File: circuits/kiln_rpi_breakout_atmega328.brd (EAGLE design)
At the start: 65 x 56 mm, 31 parts, among them Q1 5A, U1 INA125P

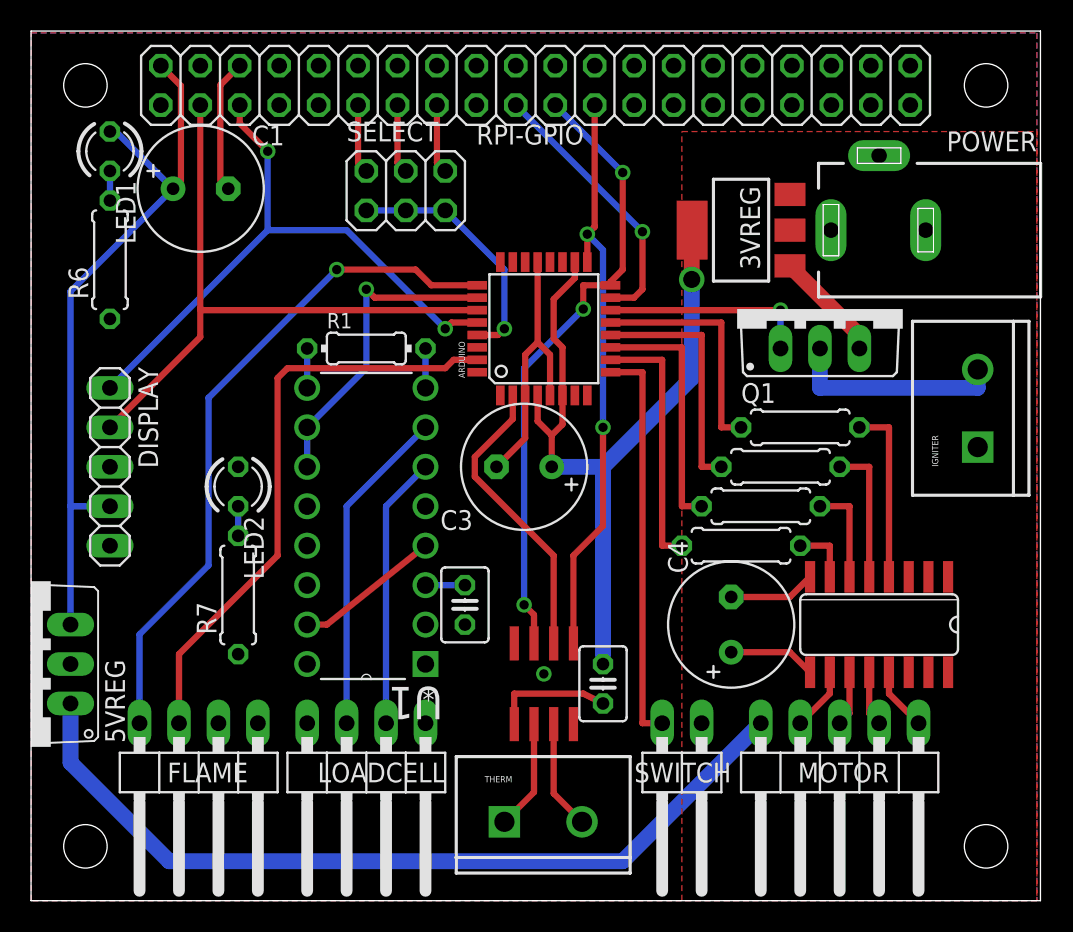
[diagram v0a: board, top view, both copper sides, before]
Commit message: Add auxtemp header, stacking power connector
Managed to update the pcb order in time. Auxtemp header takes a DS18B20
chip as an auxiliary temperature monitor, good for checking for propane
tank freezing or even as primary temperature control. Additional
powerstack header allows stacked breakouts to pass power between boards
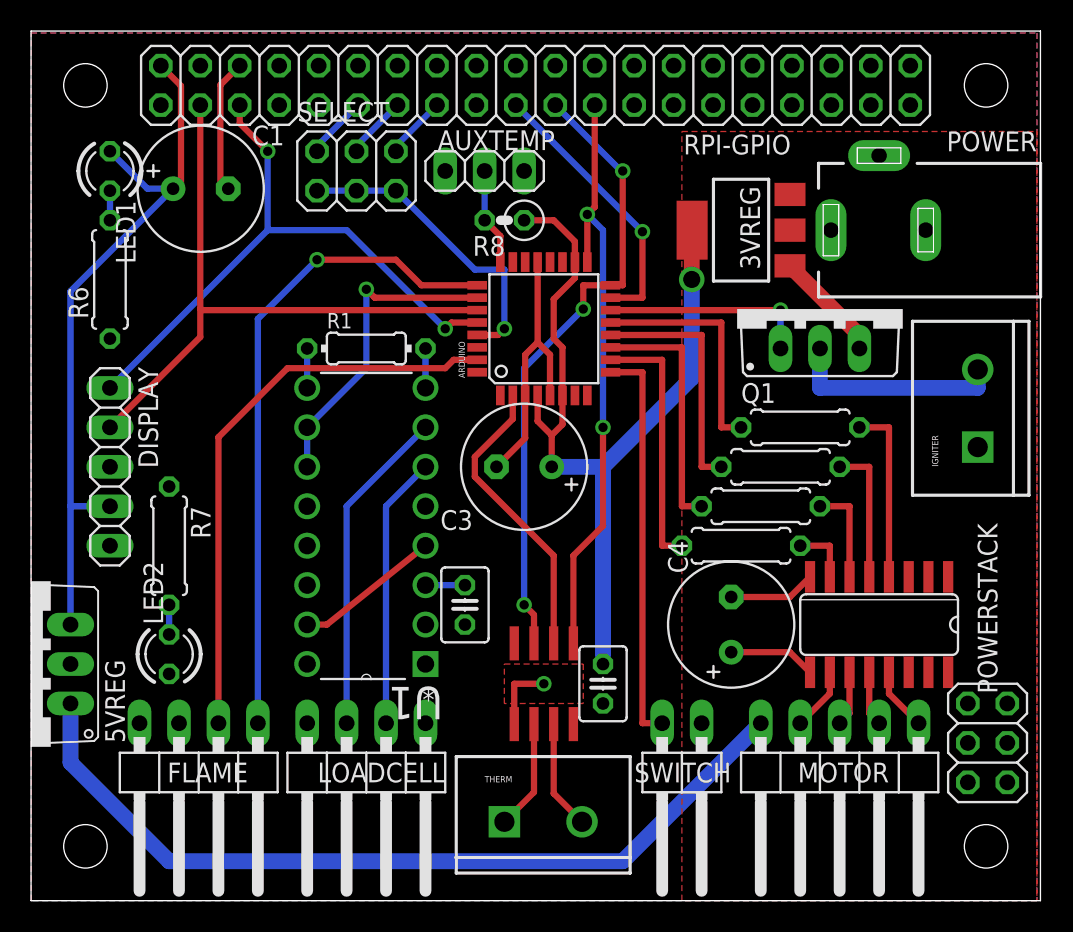
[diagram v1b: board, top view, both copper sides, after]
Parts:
- added AUXTEMP: (no value), pinhead:1X03
- added POWERSTACK: (no value), pinhead:2X03
- added R8: 4.7K, rcl:0207/2V
- moved LED2 11.7 mm to (8.89, 15.9), turned to 90 degrees
- moved R7 5.46 mm to (8.89, 22.9), turned to 270 degrees
- moved SELECT 3.42 mm to (21.0, 47.0)
- moved LED1 1.27 mm to (5.08, 47.0)
- moved R6 1.27 mm to (5.08, 40.0)
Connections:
- new net AUXTEMP: ARDUINO.24, AUXTEMP.2, R8.2
- net +3V3: now also AUXTEMP.1, FLAME.4, R8.1; no longer FLAME.1
- net FLAME_A: now also FLAME.1; no longer FLAME.4
- net FLAME_D: now also FLAME.2; no longer FLAME.3
- net GND: now also AUXTEMP.3, FLAME.3, POWERSTACK.2, POWERSTACK.4, POWERSTACK.6; no longer FLAME.2
- net V+: now also POWERSTACK.1, POWERSTACK.3, POWERSTACK.5
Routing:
- net AUXTEMP: track 0.00 -> 6.29 mm
- net +3V3: track 50.9 -> 56.0 mm
- net RESET: track 16.2 -> 19.9 mm
- net GND: track 50.1 -> 46.8 mm
- net FLAME_A: track 43.9 -> 42.4 mm
- net SCK: track 37.9 -> 39.1 mm
- net FLAME_D: track 38.2 -> 37.1 mm
- net +5V: track 47.9 -> 47.4 mm
- net MISO: track 40.4 -> 40.9 mm
- added copper zone on layer 1, net GND
